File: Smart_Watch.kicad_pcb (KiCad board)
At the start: 4 copper layers, 32 x 32 mm, 56 parts, among them J1 2169900001, J2 Conn_01x02, J3 Conn_01x06, J4 Conn_01x02, J5 Conn_01x03, J6 Conn_01x03, SW2 SW_Push, SW3 SW_Push, SW4 SW_Push, SW5 SW_Push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

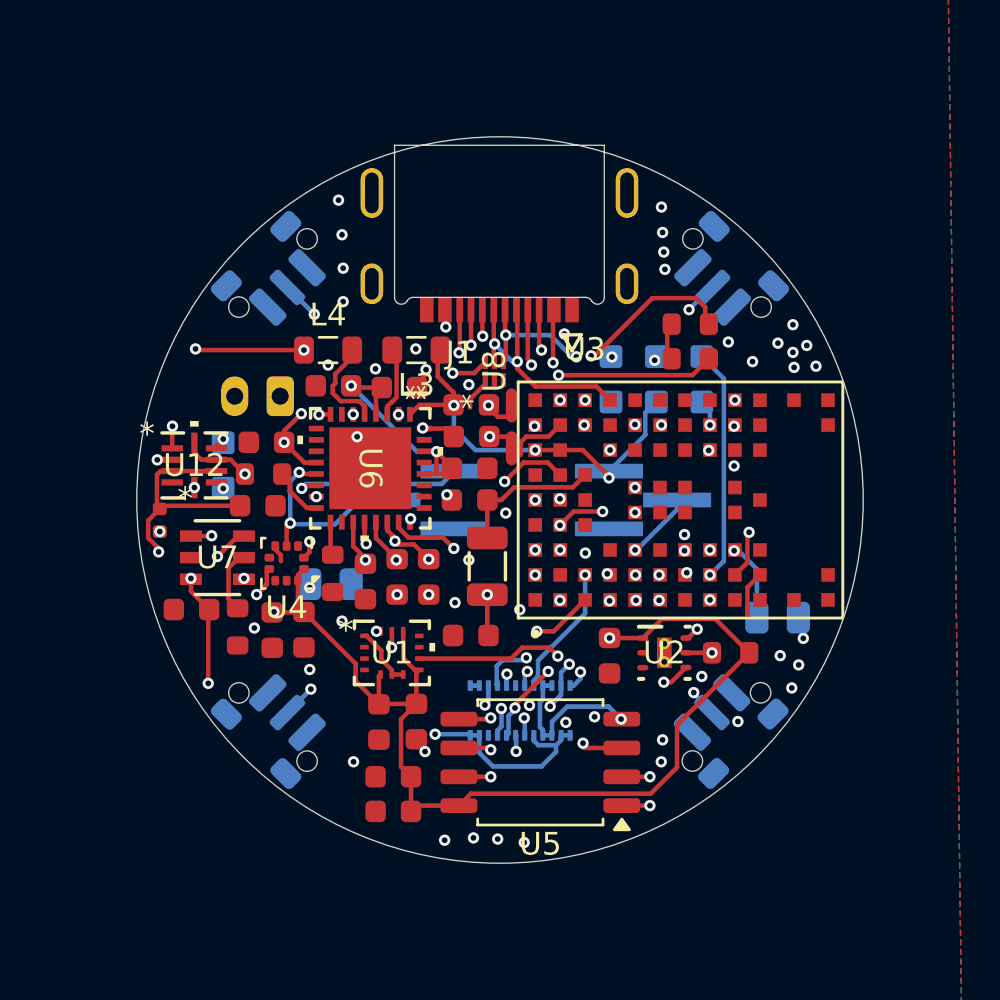
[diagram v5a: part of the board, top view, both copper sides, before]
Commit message: Updated Keepout and Started Case Model
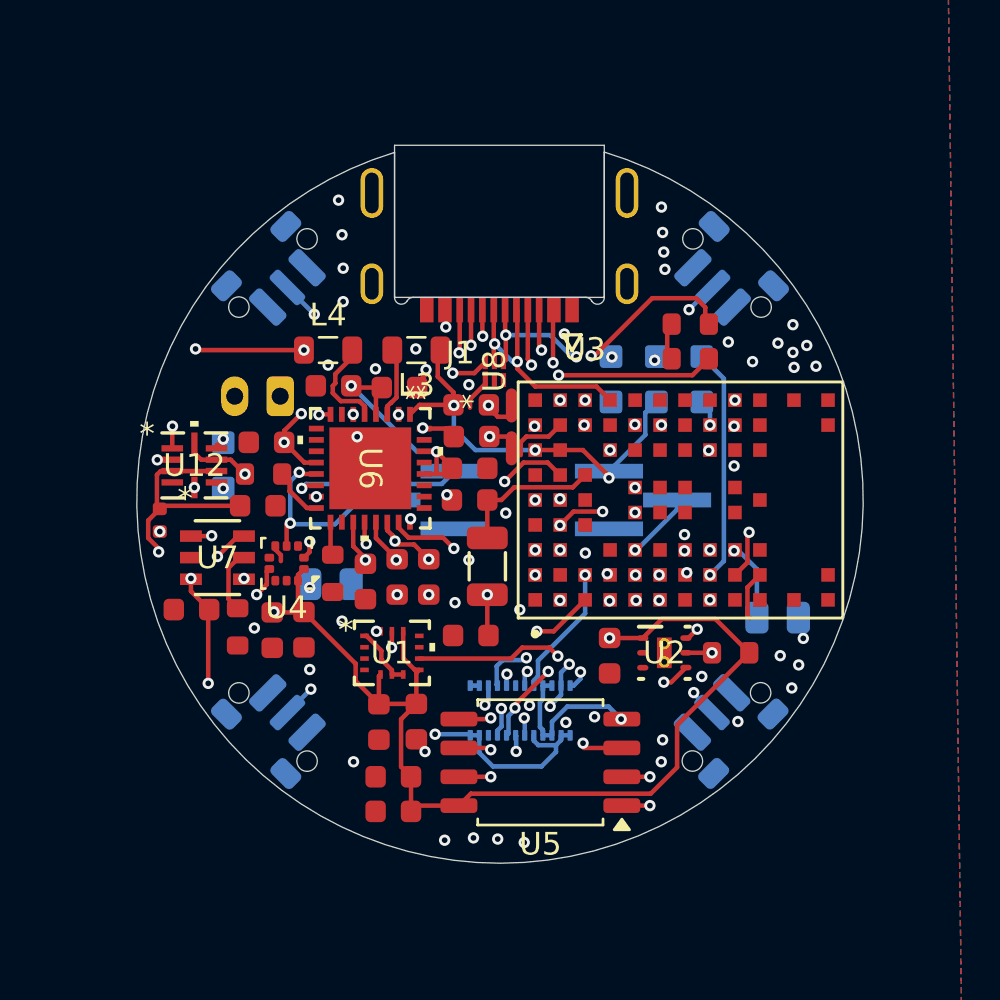
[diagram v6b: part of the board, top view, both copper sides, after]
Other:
- board size 32 x 32 mm -> 32 x 31.3 mm
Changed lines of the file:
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@@
 		(sheetname "/Architecture/MCU/")
 		(sheetfile "MCU.kicad_sch")
-		(units
-			(unit
-				(name "A")
-				(pins "J3" "C6" "B6" "C5" "B5" "D8" "E8" "E7" "D3" "B1" "C2" "C1" "B3"
-					"A2" "D2" "E2" "D1" "F2" "F1" "E1" "F3" "A5" "E3" "C8" "D7" "H1" "G3"
-					"G2" "H3" "J8" "H7" "H8" "J9" "B9" "A7" "B7" "A8" "A4" "C4" "B4" "A3"
-					"G4" "E9" "G1" "F7" "G5" "G7" "J7" "H9" "G8" "G9" "F8" "F9" "C9" "D9"
-					"J2" "H2" "A6" "J1" "J4" "J5" "K1" "K9" "A1" "A9" "B2" "B8" "E4" "E5"
-					"F4" "F5" "K2" "K3" "K5" "K7" "K8" "L1" "L9" "M1" "M2" "M8" "M9"
-				)
-			)
-		)
 		(attr smd)
 		(duplicate_pad_numbers_are_jumpers no)
@@
 			(min_thickness 0.01)
 			(keepout
-				(tracks allowed)
+				(tracks not_allowed)
 				(vias not_allowed)
-				(pads allowed)
-				(copperpour allowed)
+				(pads not_allowed)
+				(copperpour not_allowed)
 				(footprints allowed)
 			)
@@
 		)
 	)
-	(gr_circle
-		(center 172.15 107.85)
-		(end 188.15 107.85)
+	(gr_line
+		(start 167.504747 92.539166)
+		(end 167.504999 98.925)
+		(stroke
+			(width 0.05)
+			(type default)
+		)
+		(layer "Edge.Cuts")
+	)
+	(gr_line
+		(start 167.505 98.925)
+		(end 176.745 98.925001)
+		(stroke
+			(width 0.05)
+			(type default)
+		)
+		(layer "Edge.Cuts")
+	)
+	(gr_arc
+		(start 176.745 92.52401)
+		(mid 172.176244 123.849978)
+		(end 167.504747 92.539166)
+		(stroke
+			(width 0.05)
+			(type default)
+		)
+		(layer "Edge.Cuts")
+	)
+	(gr_line
+		(start 176.745 92.52401)
+		(end 176.745 98.925)
 		(stroke
 			(width 0.05)
-			(type solid)
+			(type default)
 		)
-		(fill no)
 		(layer "Edge.Cuts")
 	)
@@
 	)
 	(segment
-		(start 183.494951 108.900249)
-		(end 183.494951 101.973751)
+		(start 183.46 101.9388)
+		(end 183.2752 101.754)
 		(width 0.2)
 		(layer "In2.Cu")
@@
 	)
 	(segment
-		(start 183.1228 109.2724)
-		(end 183.494951 108.900249)
+		(start 183.46 108.9352)
+		(end 183.46 101.9388)
 		(width 0.2)
 		(layer "In2.Cu")
@@
 	)
 	(segment
-		(start 183.494951 101.973751)
-		(end 183.2752 101.754)
+		(start 183.1228 109.2724)
+		(end 183.46 108.9352)
 		(width 0.2)
 		(layer "In2.Cu")

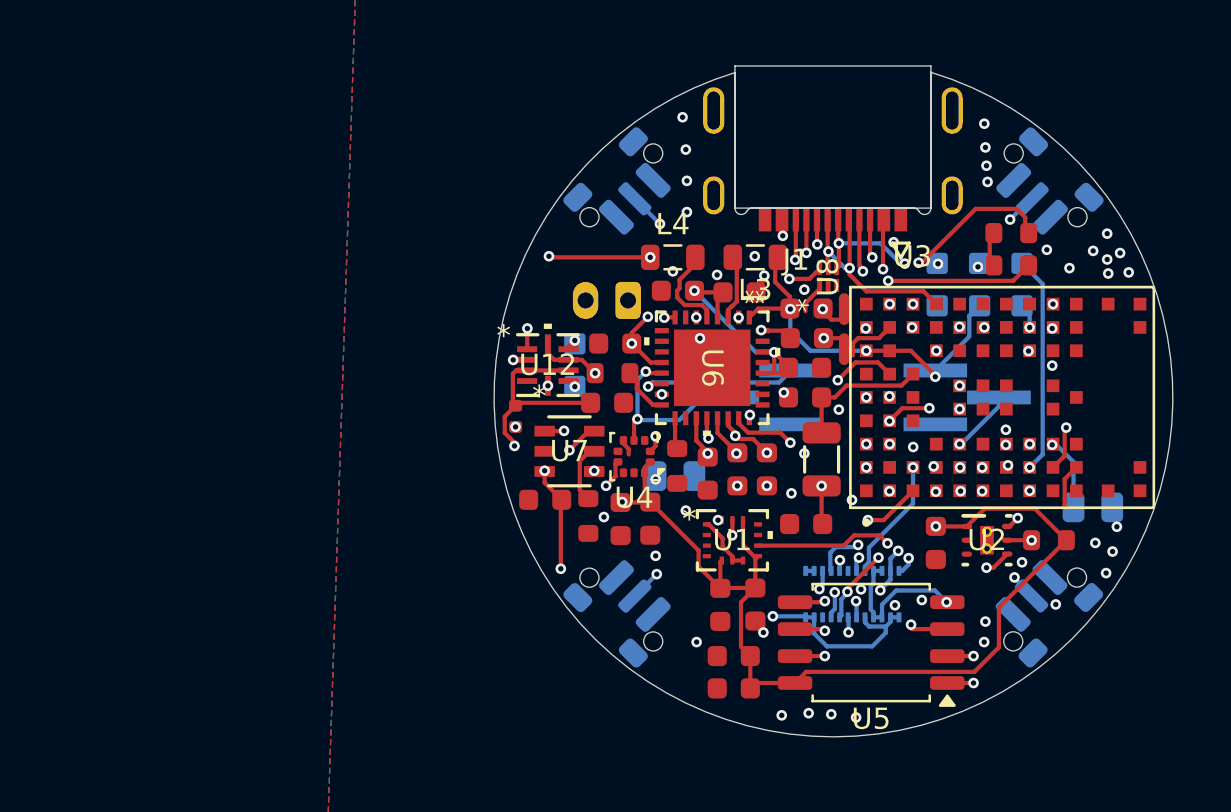
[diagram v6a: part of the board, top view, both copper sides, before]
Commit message: Began Backpack Removal to Lower Profile
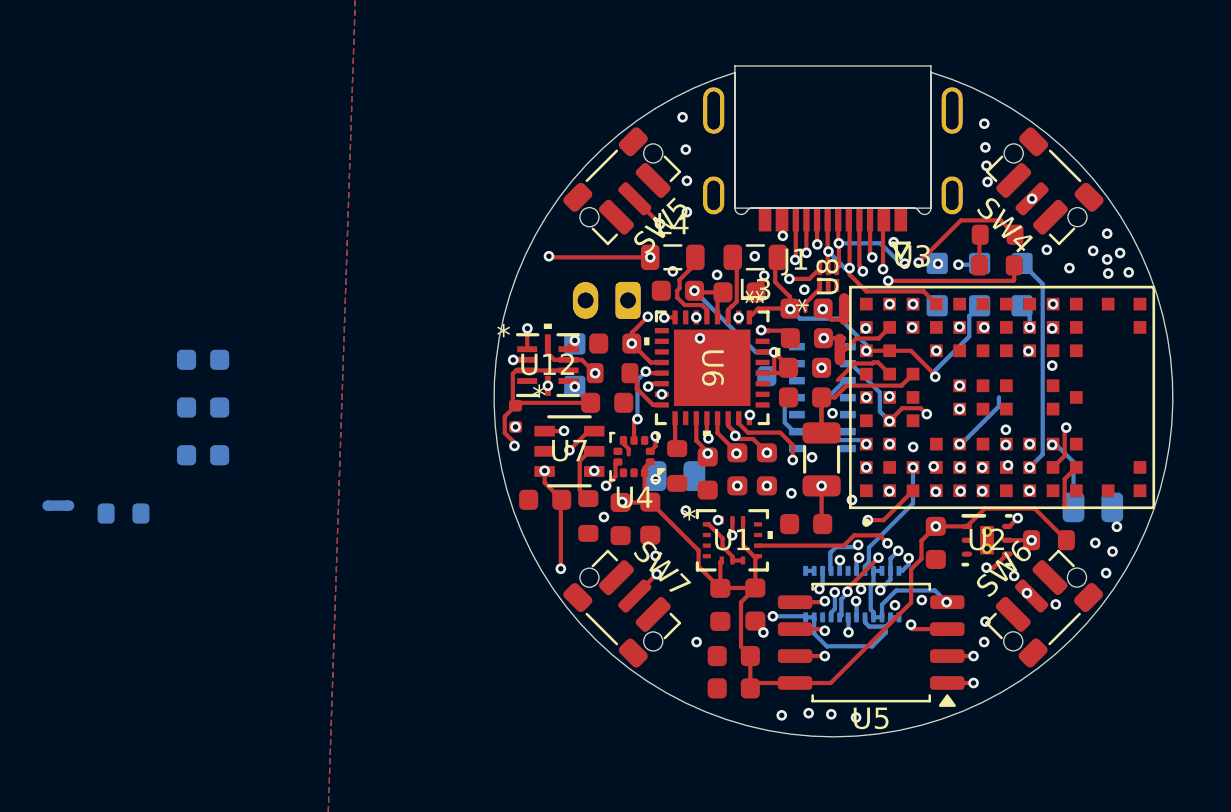
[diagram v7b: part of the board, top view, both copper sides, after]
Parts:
- removed J5, J6: Conn_01x03, Connector_PinHeader_1.27mm:PinHeader_1x03_P1.27mm_Vertical_SMD_Pin1Left
- added C1: 10uF, PCM_JLCPCB:C_0603, B.Cu at (142.4, 106.1)
- added C2: 100nF, PCM_JLCPCB:C_0603, B.Cu at (142.4, 108.3)
- added C3: 4.7uF, PCM_JLCPCB:C_0603, B.Cu at (142.4, 110.6)
- added C4: 100nF, PCM_JLCPCB:C_0603, B.Cu at (168.2, 106.8)
- added NT3: NetTie_2, NetTie:NetTie-2_SMD_Pad0.5mm, B.Cu at (135.6, 113.0)
- added R3: 4.7kΩ, PCM_JLCPCB:R_0603, B.Cu at (138.7, 113.3)
- added U9: MAX30102EFD_T, Smart_Watch:XDCR_MAX30101EFD_, B.Cu at (171.6, 107.9)
- SW4, SW5, SW6, SW7: moved to F.Cu
- moved R1 0.68 mm to (179.8, 101.6)
- moved R2 0.65 mm to (179.9, 100.2)
- moved NT2 0.21 mm to (172.4, 105.6)
- turned SW4 to 135 degrees
- turned SW5 to -135 degrees
- turned SW6 to 45 degrees
- turned SW7 to -45 degrees
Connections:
- U2 pad V: GND -> (no net)
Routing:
- net /Architecture/MCU/SCL: track 65.7 -> 61.1 mm
- net +1V8: track 83.1 -> 79.4 mm
- net /Architecture/MCU/SWCLK: track 14.2 -> 16.2 mm
- net /Architecture/MCU/CC2: track 15.2 -> 16.8 mm
- net /Architecture/MCU/CLK2: vias 2 -> 1

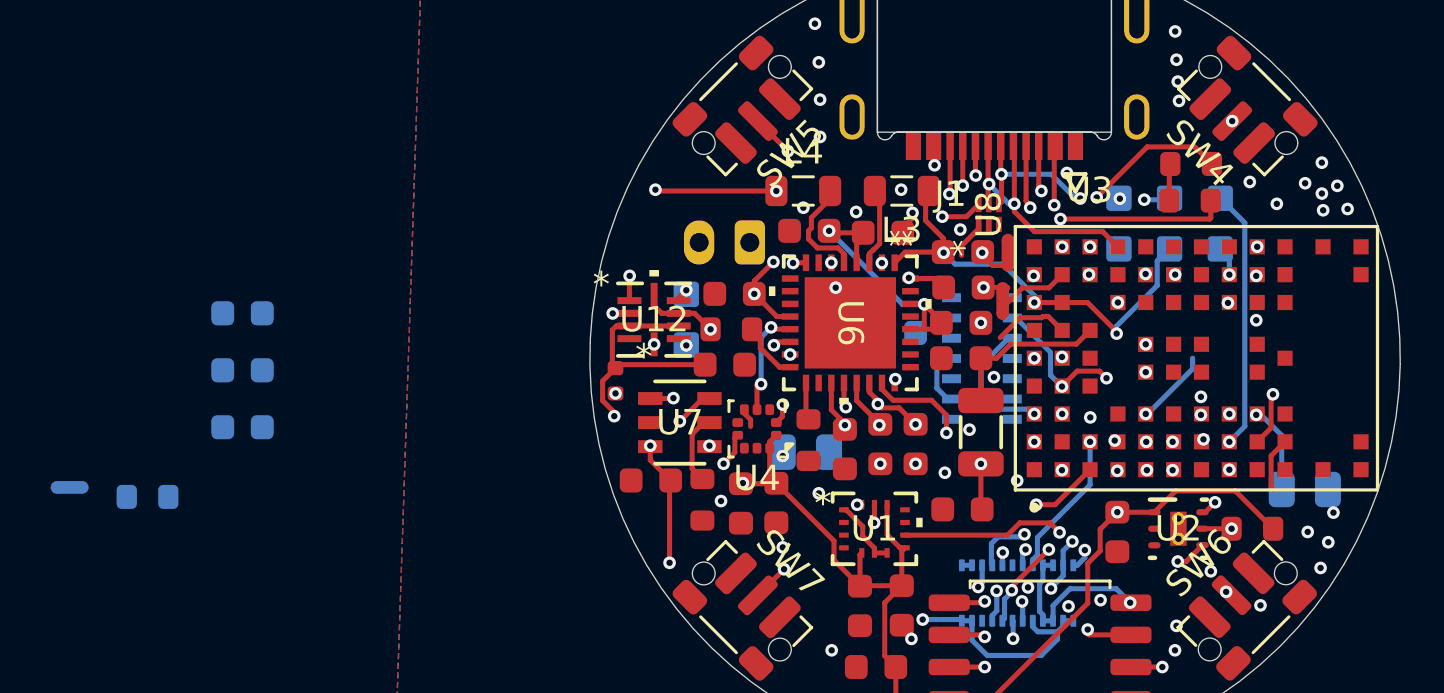
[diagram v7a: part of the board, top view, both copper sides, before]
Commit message: Flipped switches + Heart Rate, Moving Battery
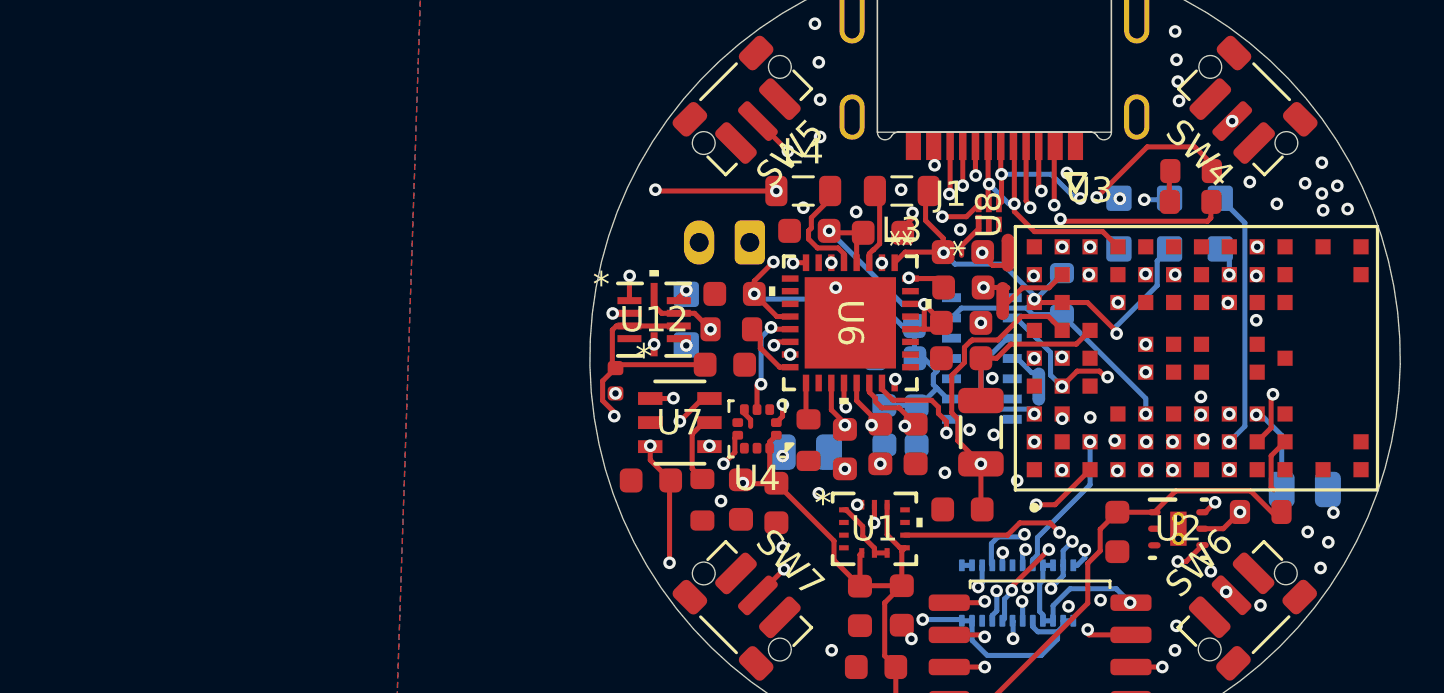
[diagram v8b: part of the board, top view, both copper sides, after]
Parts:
- moved NT3 38.5 mm to (173.9, 109.0), turned to 90 degrees
- moved R3 37.0 mm to (174.8, 105.3), turned to 90 degrees
- moved C3 26.6 mm to (169.1, 110.5), turned to -90 degrees
- moved C2 25.8 mm to (168.2, 107.8), turned to 0 degrees
- moved C1 25.7 mm to (167.8, 110.5), turned to 90 degrees
- moved R8 0.74 mm to (182.6, 113.9)
- moved R2 0.28 mm to (179.9, 100.5)
- moved C4 0.27 mm to (168.2, 106.6)
- moved C8 0.15 mm to (162.1, 113.4)
- moved R1 0.06 mm to (179.9, 101.7)
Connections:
- U2 pad V: (no net) -> GND
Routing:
- net +1V8: track 79.4 -> 92.5 mm, vias 7 -> 6
- net /Architecture/MCU/MAX_INT: track 3.01 -> 9.92 mm
- net /Architecture/MCU/CLK2: track 10.1 -> 17.0 mm
- net /Architecture/MCU/VBUS_OUT: track 19.6 -> 23.3 mm, vias 4 -> 3
- net PGND3: track 0.00 -> 1.28 mm
- net /Architecture/MCU/VBUS_IN: track 23.4 -> 24.1 mm
- net GND: vias 34 -> 35
